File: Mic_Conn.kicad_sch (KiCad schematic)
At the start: 5 parts, among them J2 JST_SH_1x4_SM04B-SRSS-TB-LF-SN, U7 TPD4E05U06QDQARQ1

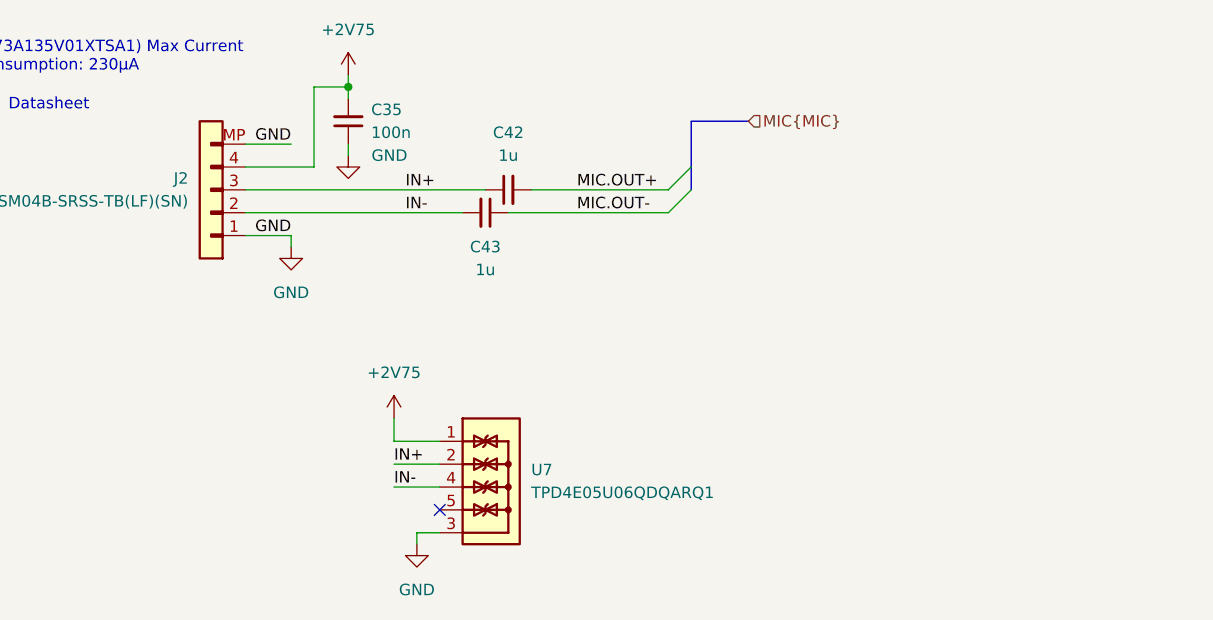
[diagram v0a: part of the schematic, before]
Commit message: [#71555] Add new root sheet structure
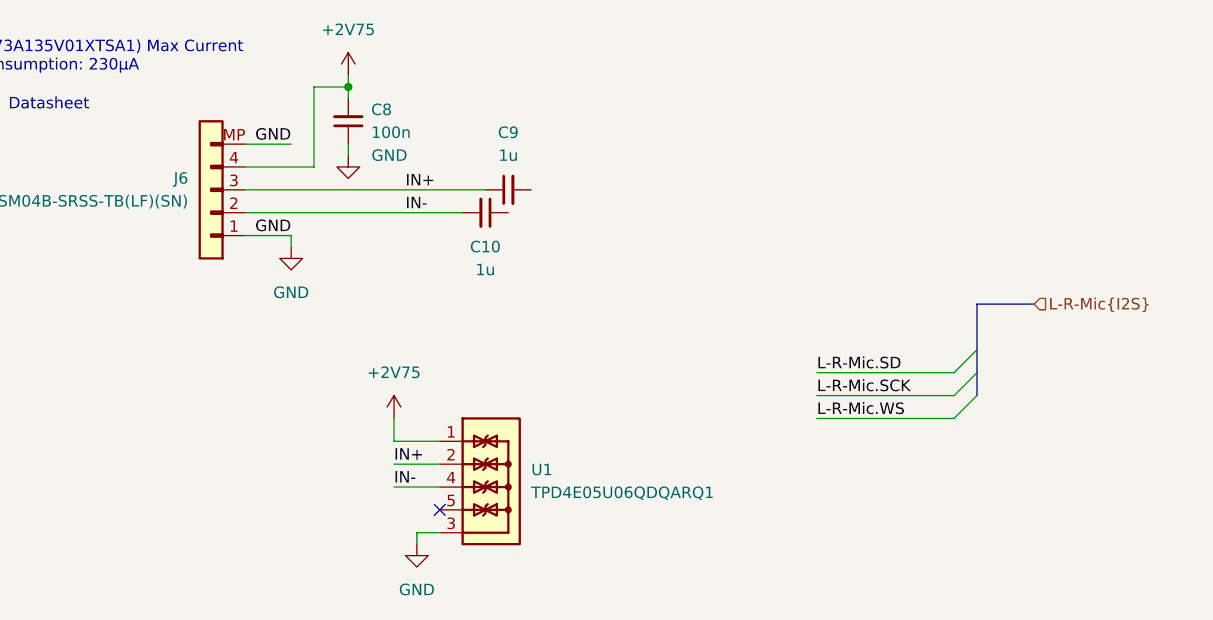
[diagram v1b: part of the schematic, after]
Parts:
- renumbered C43 to C10, C35 to C8, C42 to C9, J2 to J6, U7 to U1
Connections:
- net MIC.OUT+: no longer names the net of C9.2
- net MIC.OUT-: no longer names the net of C10.1
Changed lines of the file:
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@@
 	)
 	(bus_entry
-		(at 173.99 102.87)
+		(at 205.74 128.27)
 		(size -2.54 2.54)
 		(stroke
@@
 	)
 	(bus_entry
-		(at 173.99 105.41)
+		(at 205.74 123.19)
 		(size -2.54 2.54)
 		(stroke
@@
 		)
 	)
+	(bus_entry
+		(at 205.74 125.73)
+		(size -2.54 2.54)
+		(stroke
+			(width 0)
+			(type default)
+		)
+	)
+	(bus
+		(pts
+			(xy 212.09 118.11) (xy 205.74 118.11)
+		)
+		(stroke
+			(width 0)
+			(type default)
+		)
+	)
+	(bus
+		(pts
+			(xy 205.74 123.19) (xy 205.74 125.73)
+		)
+		(stroke
+			(width 0)
+			(type default)
+		)
+	)
 	(wire
 		(pts
@@
 	(wire
 		(pts
-			(xy 156.21 105.41) (xy 171.45 105.41)
+			(xy 187.96 125.73) (xy 203.2 125.73)
 		)
 		(stroke
@@
 	(wire
 		(pts
+			(xy 187.96 128.27) (xy 203.2 128.27)
+		)
+		(stroke
+			(width 0)
+			(type default)
+		)
+	)
+	(wire
+		(pts
 			(xy 129.54 100.33) (xy 124.46 100.33)
 		)
@@
 	(wire
 		(pts
-			(xy 153.67 107.95) (xy 171.45 107.95)
-		)
-		(stroke
-			(width 0)
-			(type default)
-		)
-	)
-	(wire
-		(pts
 			(xy 135.89 93.98) (xy 135.89 95.25)
 		)
@@
 		)
 	)
+	(bus
+		(pts
+			(xy 205.74 125.73) (xy 205.74 128.27)
+		)
+		(stroke
+			(width 0)
+			(type default)
+		)
+	)
 	(wire
 		(pts
@@
 		)
 	)
+	(wire
+		(pts
+			(xy 140.97 138.43) (xy 146.05 138.43)
+		)
+		(stroke
+			(width 0)
+			(type default)
+		)
+	)
 	(bus
 		(pts
-			(xy 173.99 97.79) (xy 180.34 97.79)
-		)
-		(stroke
-			(width 0)
-			(type default)
-		)
-	)
-	(bus
-		(pts
-			(xy 173.99 97.79) (xy 173.99 102.87)
-		)
-		(stroke
-			(width 0)
-			(type default)
-		)
-	)
-	(wire
-		(pts
-			(xy 140.97 138.43) (xy 146.05 138.43)
+			(xy 205.74 118.11) (xy 205.74 123.19)
 		)
 		(stroke
@@
 		)
 	)
-	(bus
-		(pts
-			(xy 173.99 102.87) (xy 173.99 105.41)
-		)
-		(stroke
-			(width 0)
-			(type default)
-		)
-	)
 	(wire
 		(pts
@@
 		(pts
 			(xy 140.97 135.89) (xy 146.05 135.89)
+		)
+		(stroke
+			(width 0)
+			(type default)
+		)
+	)
+	(wire
+		(pts
+			(xy 187.96 130.81) (xy 203.2 130.81)
 		)
 		(stroke
@@
 		)
 	)
-	(label "MIC.OUT+"
-		(at 161.29 105.41 0)
+	(label "GND"
+		(at 129.54 110.49 180)
 		(fields_autoplaced yes)
 		(effects
@@
 				(size 1.27 1.27)
 			)
-			(justify left bottom)
-		)
-	)
-	(label "GND"
-		(at 129.54 110.49 180)
-		(fields_autoplaced yes)
+			(justify right bottom)
+		)
+	)
+	(label "L-R-Mic.SCK"
+		(at 187.96 128.27 0)
 		(effects
 			(font
 				(size 1.27 1.27)
 			)
-			(justify right bottom)
+			(justify left bottom)
 		)
 	)
@@
 		)
 	)
-	(label "MIC.OUT-"
-		(at 161.29 107.95 0)
-		(fields_autoplaced yes)
+	(label "L-R-Mic.WS"
+		(at 187.96 130.81 0)
 		(effects
 			(font
@@
 		)
 	)
-	(label "IN-"
-		(at 140.97 138.43 0)
-		(fields_autoplaced yes)
+	(label "L-R-Mic.SD"
+		(at 187.96 125.73 0)
 		(effects
 			(font
@@
 		)
 	)
-	(label "IN+"
-		(at 142.24 105.41 0)
+	(label "IN-"
+		(at 140.97 138.43 0)
 		(fields_autoplaced yes)
 		(effects
@@
 	)
 	(label "IN+"
-		(at 140.97 135.89 0)
+		(at 142.24 105.41 0)
 		(fields_autoplaced yes)
 		(effects
@@
 		)
 	)
-	(hierarchical_label "MIC{MIC}"
+	(label "IN+"
+		(at 140.97 135.89 0)
+		(fields_autoplaced yes)
+		(effects
+			(font
+				(size 1.27 1.27)
+			)
+			(justify left bottom)
+		)
+	)
+	(hierarchical_label "L-R-Mic{I2S}"
 		(shape input)
-		(at 180.34 97.79 0)
+		(at 212.09 118.11 0)
 		(fields_autoplaced yes)
 		(effects
@@
 		(dnp no)
 		(fields_autoplaced yes)
-		(property "Reference" "#PWR051"
+		(property "Reference" "#PWR02"
 			(at 138.43 114.3 0)
 			(effects
@@
 		(instances
 			(project "audio-latency-processing-board"
-				(path "/7fb12ebf-f685-4412-b638-445b1bf344bc/66e9782a-ccab-4606-97f9-eb2618ff7d2d"
-					(reference "#PWR051")
+				(path "/7fb12ebf-f685-4412-b638-445b1bf344bc/a5973bba-065b-4f1e-8188-1e9f006e3cba"
+					(reference "#PWR02")
 					(unit 1)
 				)
@@
 		(dnp no)
 		(fields_autoplaced yes)
-		(property "Reference" "U7"
+		(property "Reference" "U1"
 			(at 156.21 136.525 0)
 			(effects
@@
 		(instances
 			(project "audio-latency-processing-board"
-				(path "/7fb12ebf-f685-4412-b638-445b1bf344bc/66e9782a-ccab-4606-97f9-eb2618ff7d2d"
-					(reference "U7")
+				(path "/7fb12ebf-f685-4412-b638-445b1bf344bc/a5973bba-065b-4f1e-8188-1e9f006e3cba"
+					(reference "U1")
 					(unit 1)
 				)
@@
 		(dnp no)
 		(fields_autoplaced yes)
-		(property "Reference" "#PWR050"
+		(property "Reference" "#PWR023"
 			(at 152.4 147.32 0)
 			(effects
@@
 		(instances
 			(project "audio-latency-processing-board"
-				(path "/7fb12ebf-f685-4412-b638-445b1bf344bc/66e9782a-ccab-4606-97f9-eb2618ff7d2d"
-					(reference "#PWR050")
+				(path "/7fb12ebf-f685-4412-b638-445b1bf344bc/a5973bba-065b-4f1e-8188-1e9f006e3cba"
+					(reference "#PWR023")
 					(unit 1)
 				)
@@
 		(on_board yes)
 		(dnp no)
-		(property "Reference" "#PWR053"
+		(property "Reference" "#PWR04"
 			(at 144.78 104.14 0)
 			(effects
@@
 		(instances
 			(project "audio-latency-processing-board"
-				(path "/7fb12ebf-f685-4412-b638-445b1bf344bc/66e9782a-ccab-4606-97f9-eb2618ff7d2d"
-					(reference "#PWR053")
+				(path "/7fb12ebf-f685-4412-b638-445b1bf344bc/a5973bba-065b-4f1e-8188-1e9f006e3cba"
+					(reference "#PWR04")
 					(unit 1)
 				)
@@
 		(dnp no)
 		(fields_autoplaced yes)
-		(property "Reference" "C43"
+		(property "Reference" "C10"
 			(at 151.1236 111.76 0)
 			(effects
@@
 		(instances
 			(project "audio-latency-processing-board"
-				(path "/7fb12ebf-f685-4412-b638-445b1bf344bc/66e9782a-ccab-4606-97f9-eb2618ff7d2d"
-					(reference "C43")
+				(path "/7fb12ebf-f685-4412-b638-445b1bf344bc/a5973bba-065b-4f1e-8188-1e9f006e3cba"
+					(reference "C10")
 					(unit 1)
 				)
@@
 		(dnp no)
 		(fields_autoplaced yes)
-		(property "Reference" "#PWR052"
+		(property "Reference" "#PWR03"
 			(at 135.89 96.52 0)
 			(effects
@@
 		(instances
 			(project "audio-latency-processing-board"
-				(path "/7fb12ebf-f685-4412-b638-445b1bf344bc/66e9782a-ccab-4606-97f9-eb2618ff7d2d"
-					(reference "#PWR052")
+				(path "/7fb12ebf-f685-4412-b638-445b1bf344bc/a5973bba-065b-4f1e-8188-1e9f006e3cba"
+					(reference "#PWR03")
 					(unit 1)
 				)
@@
 		(dnp no)
 		(fields_autoplaced yes)
-		(property "Reference" "C35"
+		(property "Reference" "C8"
 			(at 138.43 96.5136 90)
 			(effects
@@
 		(instances
 			(project "audio-latency-processing-board"
-				(path "/7fb12ebf-f685-4412-b638-445b1bf344bc/66e9782a-ccab-4606-97f9-eb2618ff7d2d"
-					(reference "C35")
+				(path "/7fb12ebf-f685-4412-b638-445b1bf344bc/a5973bba-065b-4f1e-8188-1e9f006e3cba"
+					(reference "C8")
 					(unit 1)
 				)
@@
 		(dnp no)
 		(fields_autoplaced yes)
-		(property "Reference" "J2"
+		(property "Reference" "J6"
 			(at 118.11 104.14 0)
 			(effects
@@
 		(instances
 			(project "audio-latency-processing-board"
-				(path "/7fb12ebf-f685-4412-b638-445b1bf344bc/66e9782a-ccab-4606-97f9-eb2618ff7d2d"
-					(reference "J2")
+				(path "/7fb12ebf-f685-4412-b638-445b1bf344bc/a5973bba-065b-4f1e-8188-1e9f006e3cba"
+					(reference "J6")
 					(unit 1)
 				)
@@
 		(dnp no)
 		(fields_autoplaced yes)
-		(property "Reference" "#PWR049"
+		(property "Reference" "#PWR05"
 			(at 140.97 134.62 0)
 			(effects
@@
 		(instances
 			(project "audio-latency-processing-board"
-				(path "/7fb12ebf-f685-4412-b638-445b1bf344bc/66e9782a-ccab-4606-97f9-eb2618ff7d2d"
-					(reference "#PWR049")
+				(path "/7fb12ebf-f685-4412-b638-445b1bf344bc/a5973bba-065b-4f1e-8188-1e9f006e3cba"
+					(reference "#PWR05")
 					(unit 1)
 				)
@@
 		(dnp no)
 		(fields_autoplaced yes)
-		(property "Reference" "C42"
+		(property "Reference" "C9"
 			(at 153.6763 99.06 0)
 			(effects
@@
 		(instances
 			(project "audio-latency-processing-board"
-				(path "/7fb12ebf-f685-4412-b638-445b1bf344bc/66e9782a-ccab-4606-97f9-eb2618ff7d2d"
-					(reference "C42")
+				(path "/7fb12ebf-f685-4412-b638-445b1bf344bc/a5973bba-065b-4f1e-8188-1e9f006e3cba"
+					(reference "C9")
 					(unit 1)
 				)

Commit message: [#71555] Draw MIC and USB Connector sheets
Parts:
- removed C10, C9: C_1u_0402, antmicro-footprints:C_0402_1005Metric, symbol antmicroCapacitors0402:C_1u_0402
- removed C8: C_100n_0402, antmicro-footprints:C_0402_1005Metric, symbol antmicroCapacitors0402:C_100n_0402
- removed J6: JST_SH_1x4_SM04B-SRSS-TB-LF-SN, antmicro-footprints:Conn_JST_SH_1x4_SM04B-SRSS-TB-LF-SN, symbol antmicroWire2BoardConnectors:JST_SH_1x4_SM04B-SRSS-TB-LF-SN
- added C4, C5: C_100n_0402, antmicro-footprints:C_0402_1005Metric, symbol antmicroCapacitors0402:C_100n_0402
- added J1, J2: JST_SUR_1x5_BM05B-SURS-TB-LF-SN, antmicro-footprints:Conn_JST_SUR_1x5_BM05B-SURS-TF-LF-SN, symbol antmicroWire2BoardConnectors:JST_SUR_1x5_BM05B-SURS-TB-LF-SN
- added R18, R19, R20, R21, R22, R23, R24, R25, R3, R4: R_0R_0402, antmicro-footprints:R_0402_1005Metric, symbol antmicroResistors0402:R_0R_0402
- added U6: TPD4E05U06QDQARQ1, antmicro-footprints:USON-10_2.5x1mm_P0.5mm, symbol antmicroTVSDiodes:TPD4E05U06QDQARQ1
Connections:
- net GND: now also C4.1, C5.1, J1.2, J1.MP, J2.2, J2.MP, U6.3, U6.8
- net L-R-Mic.SCK: now also R22.2, R23.2
- net L-R-Mic.SD: now also R20.2, R21.2
- net L-R-Mic.WS: now also R24.2, R25.2
- net L-DATA: now reaches U1.5, U1.6
- net L-DATA: now also J1.5, R20.1
- net +2V75 renamed L-PWR
- net L-PWR: now also C5.2, J1.1, R18.1, R19.1
- net IN+ renamed L-BCLK
- net L-BCLK: now also J1.3, R22.1
- net IN- renamed L-WS
- net L-WS: now also J1.4, R24.1
- new net +1V8: R19.2, R3.2
- new net +3V3: R18.2, R4.2
- new net R-BCLK: J2.3, R23.1, U6.2, U6.9
- new net R-DATA: J2.5, R21.1, U6.5, U6.6
- new net R-PWR: C4.2, J2.1, R3.1, R4.1, U6.1, U6.10
- new net R-WS: J2.4, R25.1, U6.4, U6.7
- no-connect marks 1 -> 0
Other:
- note added: "Microphone (SPH0645LM4H-B) Typ. current: 600µA"
- note removed: "Microphone (IM73A135V01XTSA1) Max Current consumption: 230µA"

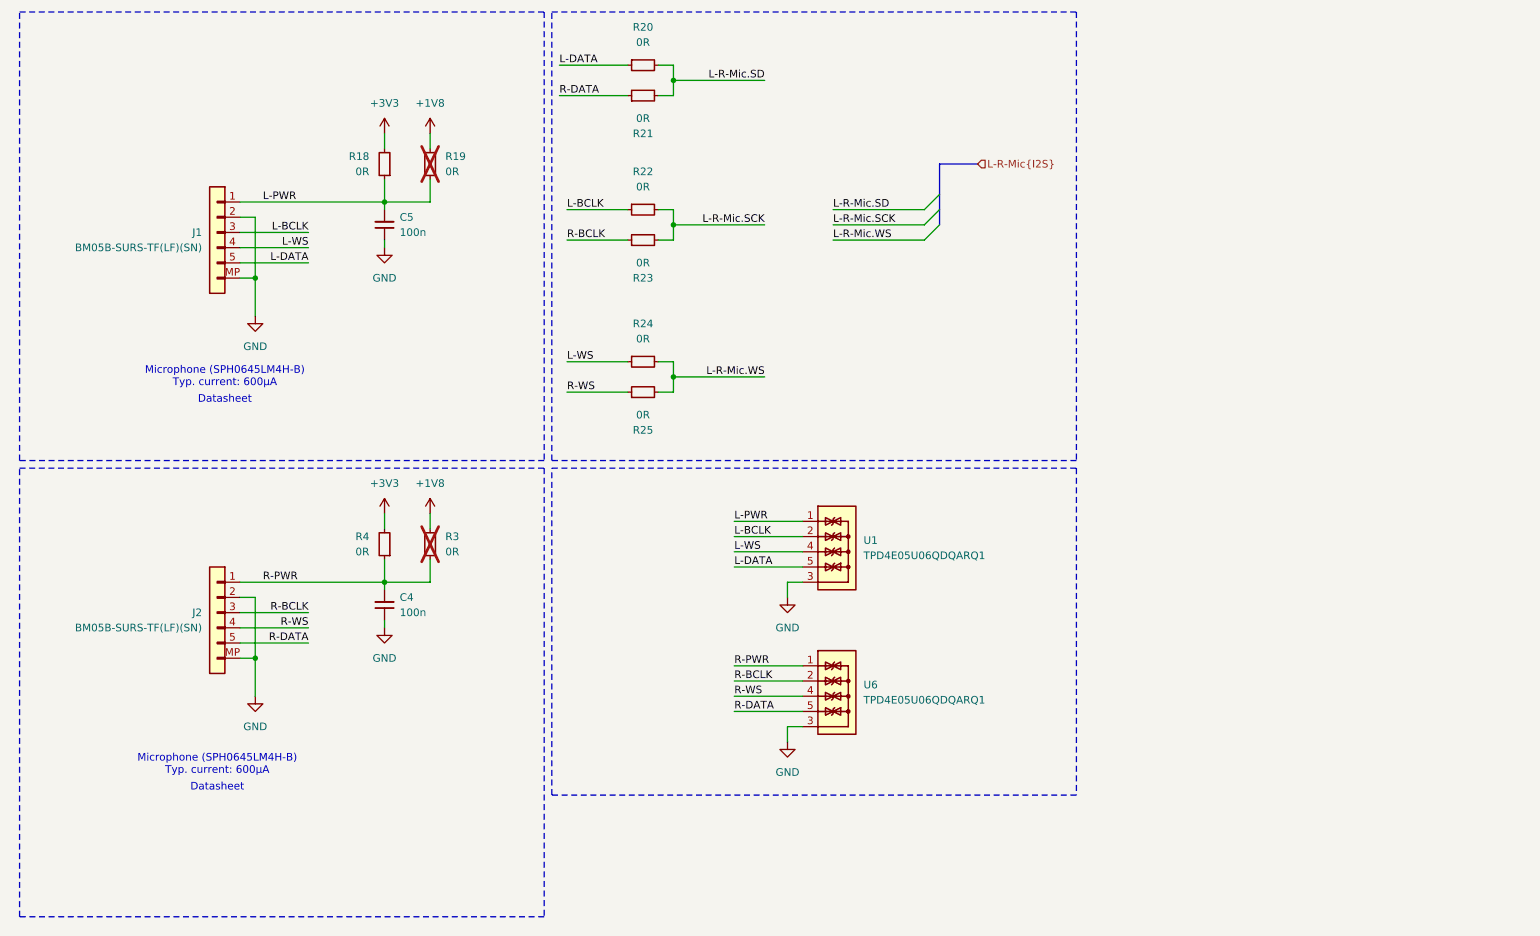
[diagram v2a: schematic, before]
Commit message: [#71555] Add connections between RP2040s
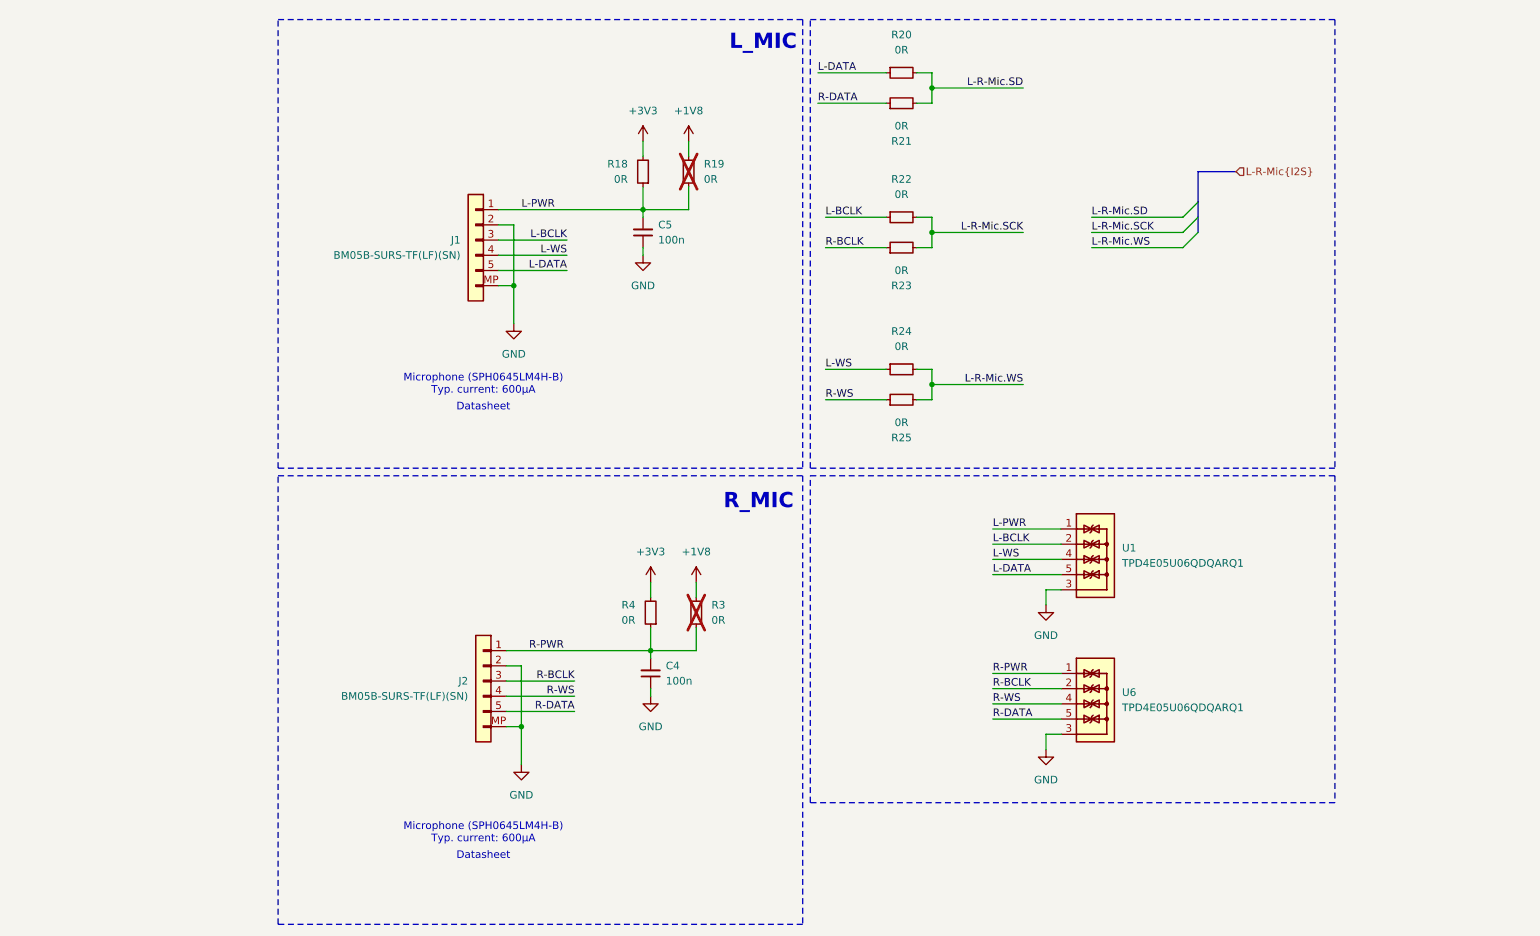
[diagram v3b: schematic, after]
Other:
- note added: "L_MIC"
- note added: "R_MIC"
- moved on the sheet: C4, C5, J1, J2, R18, R19, R20, R21, R22, R23, R24, R25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
